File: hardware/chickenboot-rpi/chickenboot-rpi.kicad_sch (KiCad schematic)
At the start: 40 parts, among them J1 USB_C_Receptacle_USB2.0, J2 Conn_01x03, J3 Conn_01x03, J4 JTAG, Q1 LP0404N3T5G, SW1 SW_Push, SW2 SW_Push, U1 RP2350_60QFN, U2 HT7533-1, U3 USBLC6-2P6, Y1 12MHz

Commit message: add a decouliping capacitor to flash, a pullup to PMOS power control, and clean schematics
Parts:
- U1: value RP2350_60QFN -> RP2354_60QFN; footprint RP2350_60QFN_minimal:RP2350-QFN-60-1EP_7x7_P0.4mm_EP3.4x3.4mm_ThermalVias -> RP2354_60QFN_minimal:RP2350-QFN-60-1EP_7x7_P0.4mm_EP3.4x3.4mm_ThermalVias
- renumbered R2 to R3
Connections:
- net GPIO10: no longer TP1.1
- net GPIO8: now also TP1.1
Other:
- note added: "DECOUPLING"
- note added: "I/O HEADERS"
- note added: "MCU"
- note added: "POWER"
- note added: "USB Connector"
- note removed: "Make sure R7 and R8 are close to RP2350"
- company: Raspberry Pi Ltd -> (C) 2026 Victor Suarez Rovere
- title: RP2350A QFN-60 Minimal Design Example -> ChickenBoot
- moved on the sheet: C10, C11, C12, C13, C14, C15, C16, C17, C18, C2, C6, C7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

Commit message: clean schematics and version match between schematics and PCB
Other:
- moved on the sheet: C1, C2, C6, C7, C9, L1, LED1, R4, R5, U2

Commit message: add BOM/POS for manufacturing and related fixes
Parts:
- removed C10, C9: 4.7u, Capacitor_SMD:C_0402_1005Metric, symbol Device:C
- removed C7: 4.7u, RP2350_60QFN_minimal:C_0402_1005Metric_small_pads, symbol Device:C
- removed J4: JTAG, Connector_IDC:IDC-Header_2x03_P2.54mm_Vertical, symbol PRT-12807:PRT-12807
- removed Q1: LP0404N3T5G, Package_TO_SOT_SMD:SOT-883, symbol Seeed_libadl:Mosfet/305031466
- added C3, C5: 4.7u, RP2350_60QFN_minimal:C_0402_1005Metric_small_pads, symbol Device:C
- added C4: 4.7u 10V, RP2350_60QFN_minimal:C_0402_1005Metric_small_pads, symbol Device:C
- added CN1: 69168-106HLF, easyeda2kicad:CONN-TH_6P-P2.54_69168-X06, symbol easyeda2kicad:69168-106HLF
- added Q2: WPM2093-3/TR, easyeda2kicad:SOT-723_L1.2-W0.8-P0.80-LS1.2-BR, symbol easyeda2kicad:WPM2093-3_TR
- C6: value 4.7u -> 4.7u 10V; MPN (none) -> CL05A475KP5NRNC
- L1: LCSC Part Number (none) -> C42411119
- SW1, SW2: LCSC Part C41398745 -> (none); LCSC Part Number (none) -> C41398745
- U1: LCSC Part Number (none) -> C41378174
- U3: LCSC Part Number (none) -> C15999; MPN (none) -> USBLC6-2P6
- Y1: LCSC Part Number (none) -> C54307921
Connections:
- net +1V1: now also C4.1, C5.1
- net +3V3: now also Q2.2 (S)
- net GND: now also C3.2, C4.2, C5.2, CN1.3
- net GPIO25: now also Q2.1 (G)
- net JTAG_TCK: now also CN1.5
- net JTAG_TDI: now also CN1.2
- net JTAG_TDO: now also CN1.4
- net JTAG_TMS: now also CN1.6
- net TARGET_VCC: now also CN1.1, Q2.3 (D)
- net VREG_AVDD: now also C3.1
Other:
- moved on the sheet: R10

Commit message: change boards shape and fixes for manufacturability
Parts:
- CN1: LCSC Part C5410110 -> (none); LCSC Part Number (none) -> C5410110
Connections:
- net GND: now also J3.1 (Pin_1); no longer J3.3 (Pin_3)
- net RX: now also J3.3 (Pin_3); no longer J3.1 (Pin_1)
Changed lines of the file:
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@@
 		(lib_id "Connector_Generic:Conn_01x03")
 		(at 337.82 102.235 0)
+		(mirror x)
 		(unit 1)
 		(exclude_from_sim no)
@@
 		(dnp yes)
 		(property "Reference" "J3"
-			(at 337.82 95.758 0)
+			(at 337.82 108.712 0)
 			(effects
 				(font
@@
 		)
 		(property "Value" "Conn_01x03"
-			(at 337.82 108.585 0)
+			(at 337.82 95.885 0)
 			(effects
 				(font
@@
 			)
 		)
-		(property "LCSC Part" "C5410110"
+		(property "LCSC Part Number" "C5410110"
 			(at 342.9 100.33 0)
 			(effects

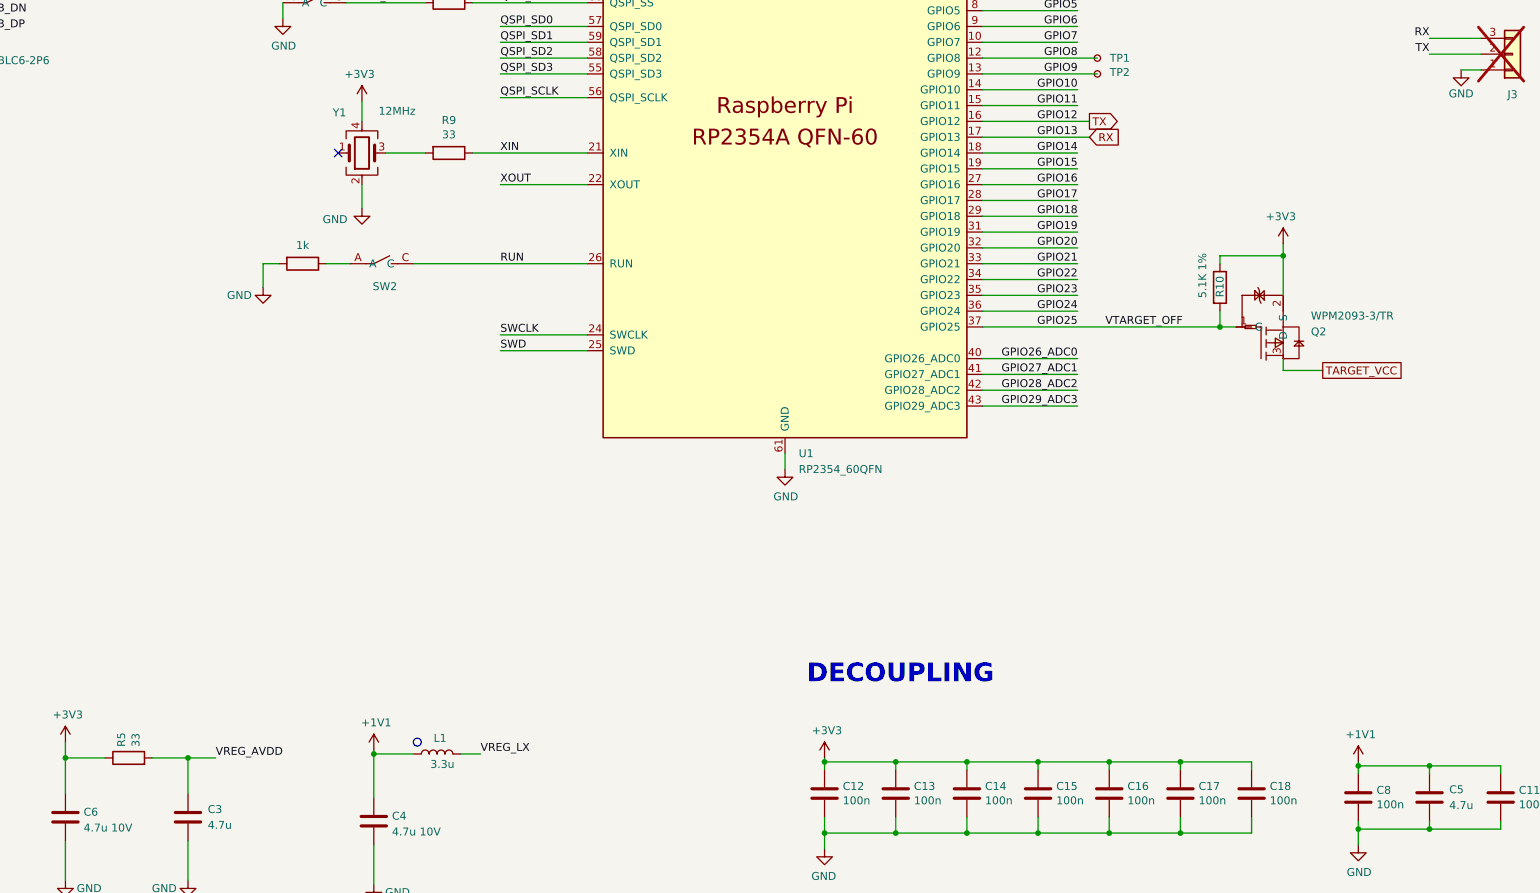
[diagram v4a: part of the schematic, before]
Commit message: add status led and use all 27R instead of 33R to optimize components
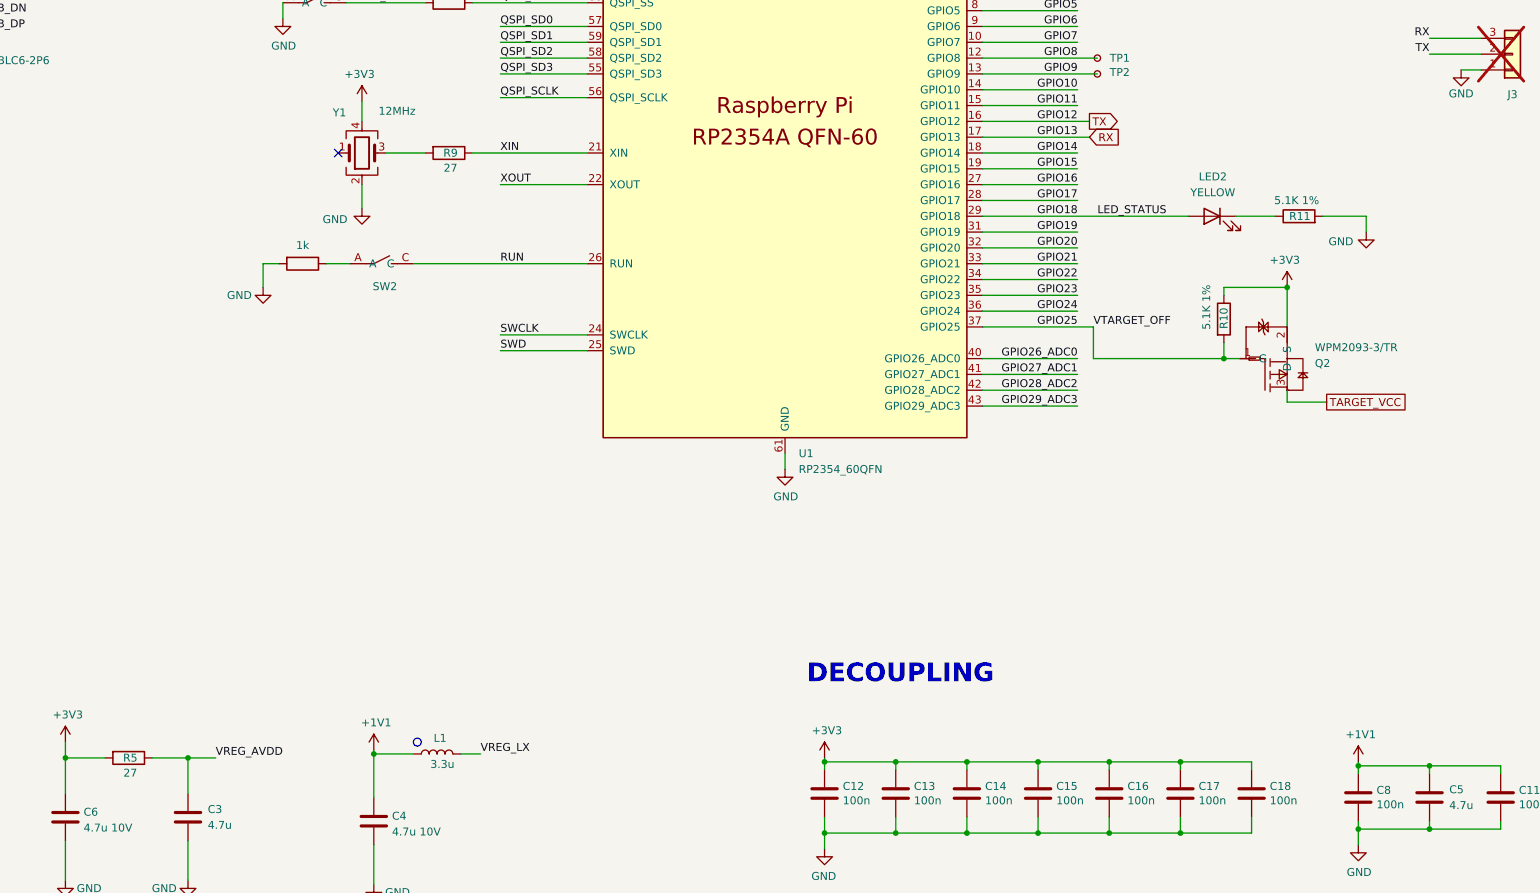
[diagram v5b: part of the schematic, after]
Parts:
- added LED2: YELLOW, LED_SMD:LED_0603_1608Metric, symbol Device:LED
- added R11: 5.1K 1%, Resistor_SMD:R_0402_1005Metric, symbol Device:R
- R5, R9: value 33 -> 27
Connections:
- net +3V3: now also R5.2; no longer R5.1
- net GND: now also R11.2
- net GPIO18: now also LED2.2 (A)
- net VREG_AVDD: now also R5.1; no longer R5.2
- new net: LED2.1 (K), R11.1
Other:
- moved on the sheet: Q2, R10
